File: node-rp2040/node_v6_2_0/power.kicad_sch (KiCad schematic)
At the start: 19 parts, among them J10 Connector, USB-TYPE-C-16P, Q1 DMG2301L, U3 AP2112K-3.3, U5 MCP73831-2-OT

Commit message: finished layout v6.2
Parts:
- R17, R18: footprint JLCPCB:R_0805 -> JLCPCB:R_0603
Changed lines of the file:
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@@
 			)
 		)
-		(property "Footprint" "JLCPCB:R_0805"
+		(property "Footprint" "JLCPCB:R_0603"
 			(at 26.162 54.61 90)
 			(effects
@@
 			)
 		)
-		(property "Footprint" "JLCPCB:R_0805"
+		(property "Footprint" "JLCPCB:R_0603"
 			(at 26.162 44.45 90)
 			(effects

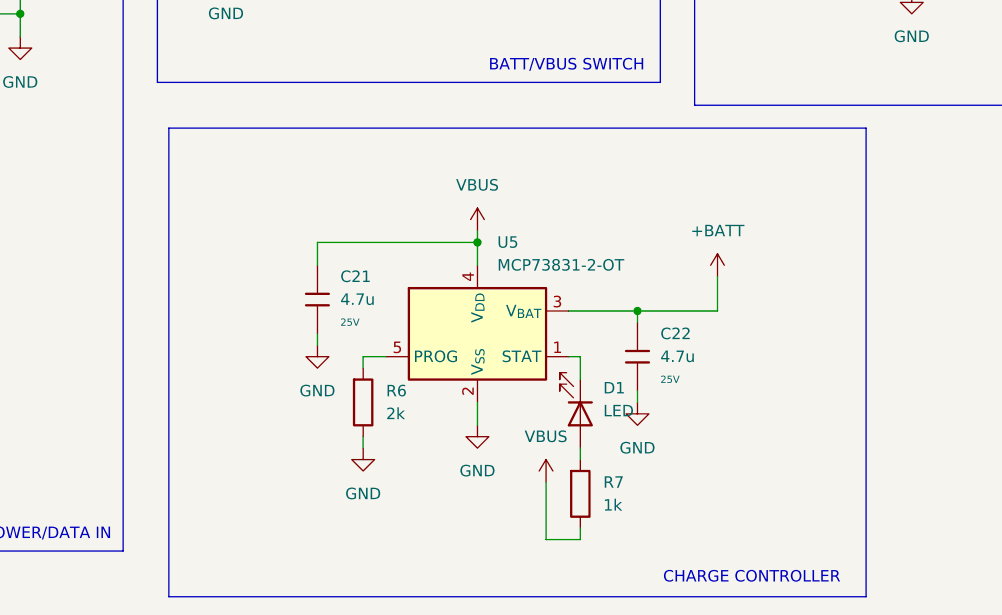
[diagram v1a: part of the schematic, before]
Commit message: added zener diode for overvoltage protection on vbus, small routing adjustments, silkscreen component labels
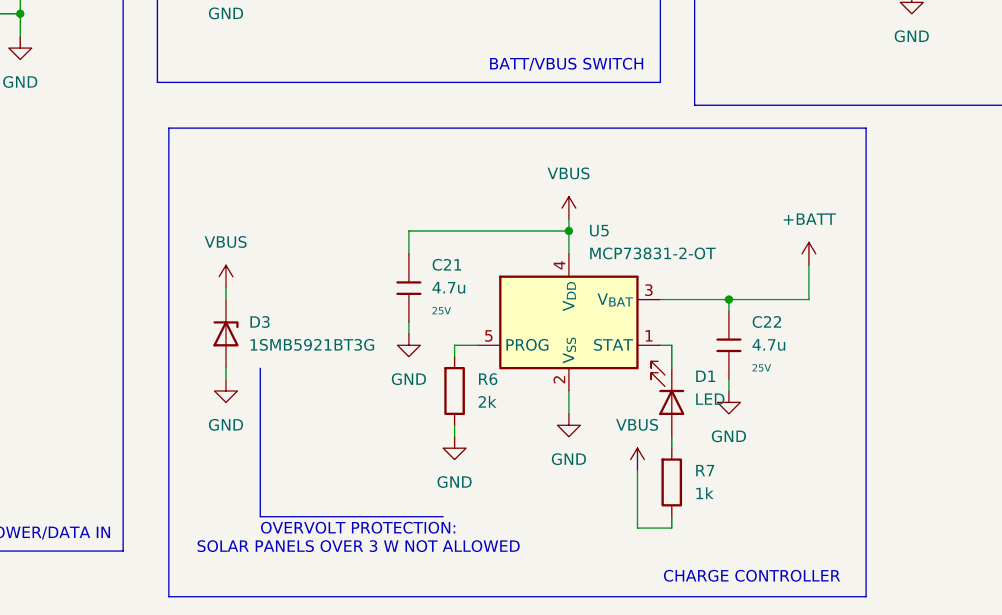
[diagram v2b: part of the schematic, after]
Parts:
- added D3: 1SMB5921BT3G, JLCPCB:D_SMB, symbol Device:D_Zener
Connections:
- net GND: now also D3.2 (A)
- net VBUS: now also D3.1 (K)
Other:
- note added: "OVERVOLT PROTECTION: SOLAR PANELS OVER 3 W NOT ALLOWED"
- moved on the sheet: C21, C22, D1, R6, R7, U5
